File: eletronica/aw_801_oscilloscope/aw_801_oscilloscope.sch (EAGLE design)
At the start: 2 parts

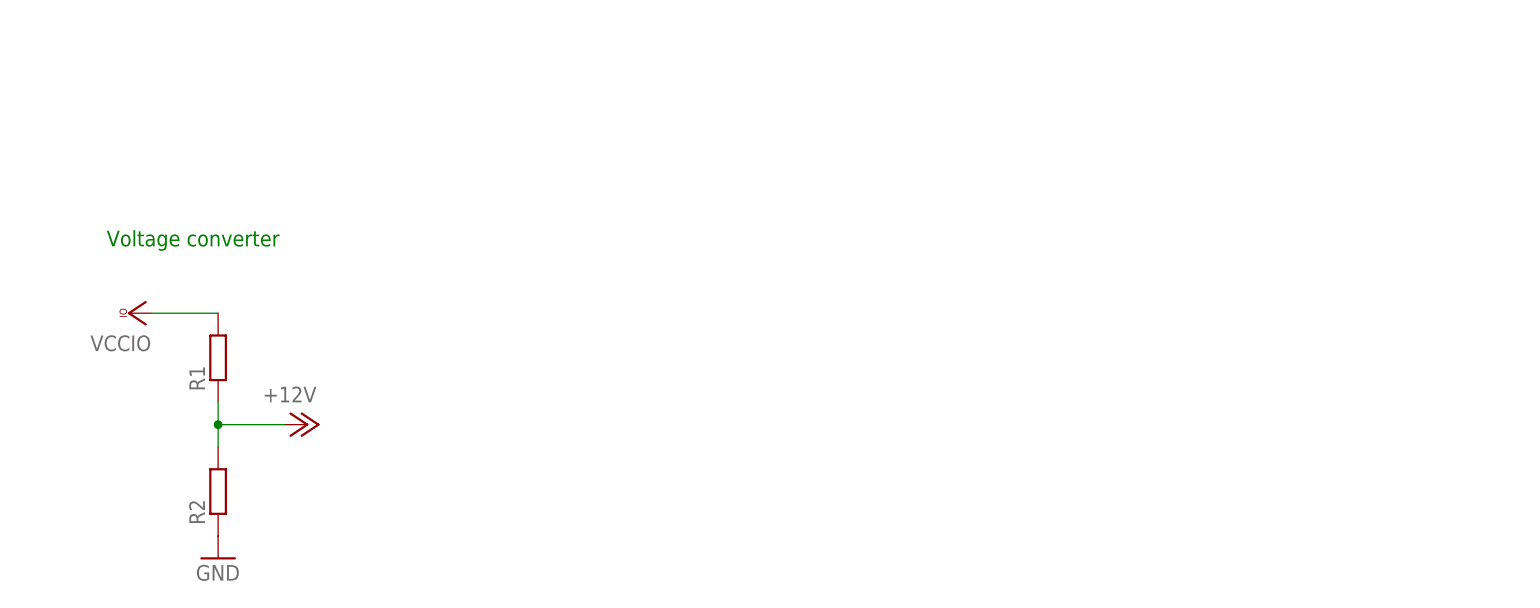
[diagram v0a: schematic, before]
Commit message: 
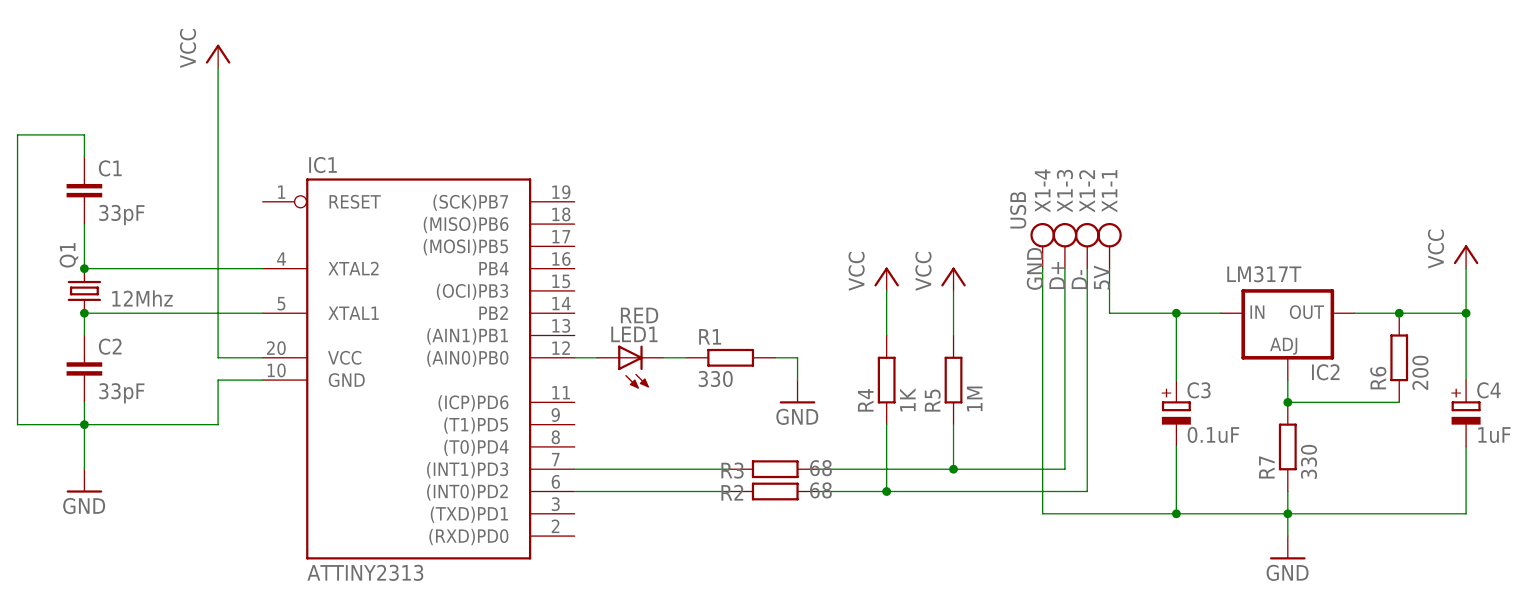
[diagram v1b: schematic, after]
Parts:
- added C1, C2: 33pF, rcl:C-EU050-030X075
- added C3: 0.1uF, rcl:CPOL-EUE2.5-6
- added C4: 1uF, rcl:CPOL-EUE2.5-6
- added IC1: ATTINY2313, atmel:AT90S2313P
- added IC2: LM317T, v-reg:LM317TS
- added LED1: RED, led:LED5MM
- added Q1: 12Mhz, crystal:CRYSTALHC49U70
- added R3: 68, rcl:R-EU_0207/10
- added R4: 1K, rcl:R-EU_0207/10
- added R5: 1M, rcl:R-EU_0207/10
- added R6: 200, rcl:R-EU_0207/10
- added R7: 330, rcl:R-EU_0207/10
- added X1: USB, con-ptr500:AK500/4
- R1: value (none) -> 330; device rcl:R-EU_0207/7 -> rcl:R-EU_0207/10
- R2: value (none) -> 68; device rcl:R-EU_0207/7 -> rcl:R-EU_0207/10
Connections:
- removed net +12V: R1.1, R2.2
- removed net VCCIO: R1.2
- new net 5V: C3.+, IC2.IN, X1-1.KL
- new net D+: R3.2, R5.1, X1-3.KL
- new net D-: R2.2, R4.1, X1-2.KL
- new net N$1: C1.2, IC1.XTAL2, Q1.2
- new net N$2: C2.1, IC1.XTAL1, Q1.1
- new net N$3: IC1.(AIN0)PB0, LED1.A
- new net N$4: LED1.C, R1.1
- new net N$5: IC1.(INT0)PD2, R2.1
- new net N$6: IC1.(INT1)PD3, R3.1
- new net N$9: IC2.ADJ, R6.1, R7.2
- new net VCC: C4.+, IC1.VCC, IC2.OUT, R4.2, R5.2, R6.2
- net GND: now also C1.1, C2.2, C3.-, C4.-, IC1.GND, R1.2, R7.1, X1-4.KL; no longer R2.1
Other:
- note removed: "Voltage converter"
- moved on the sheet: R1, R2

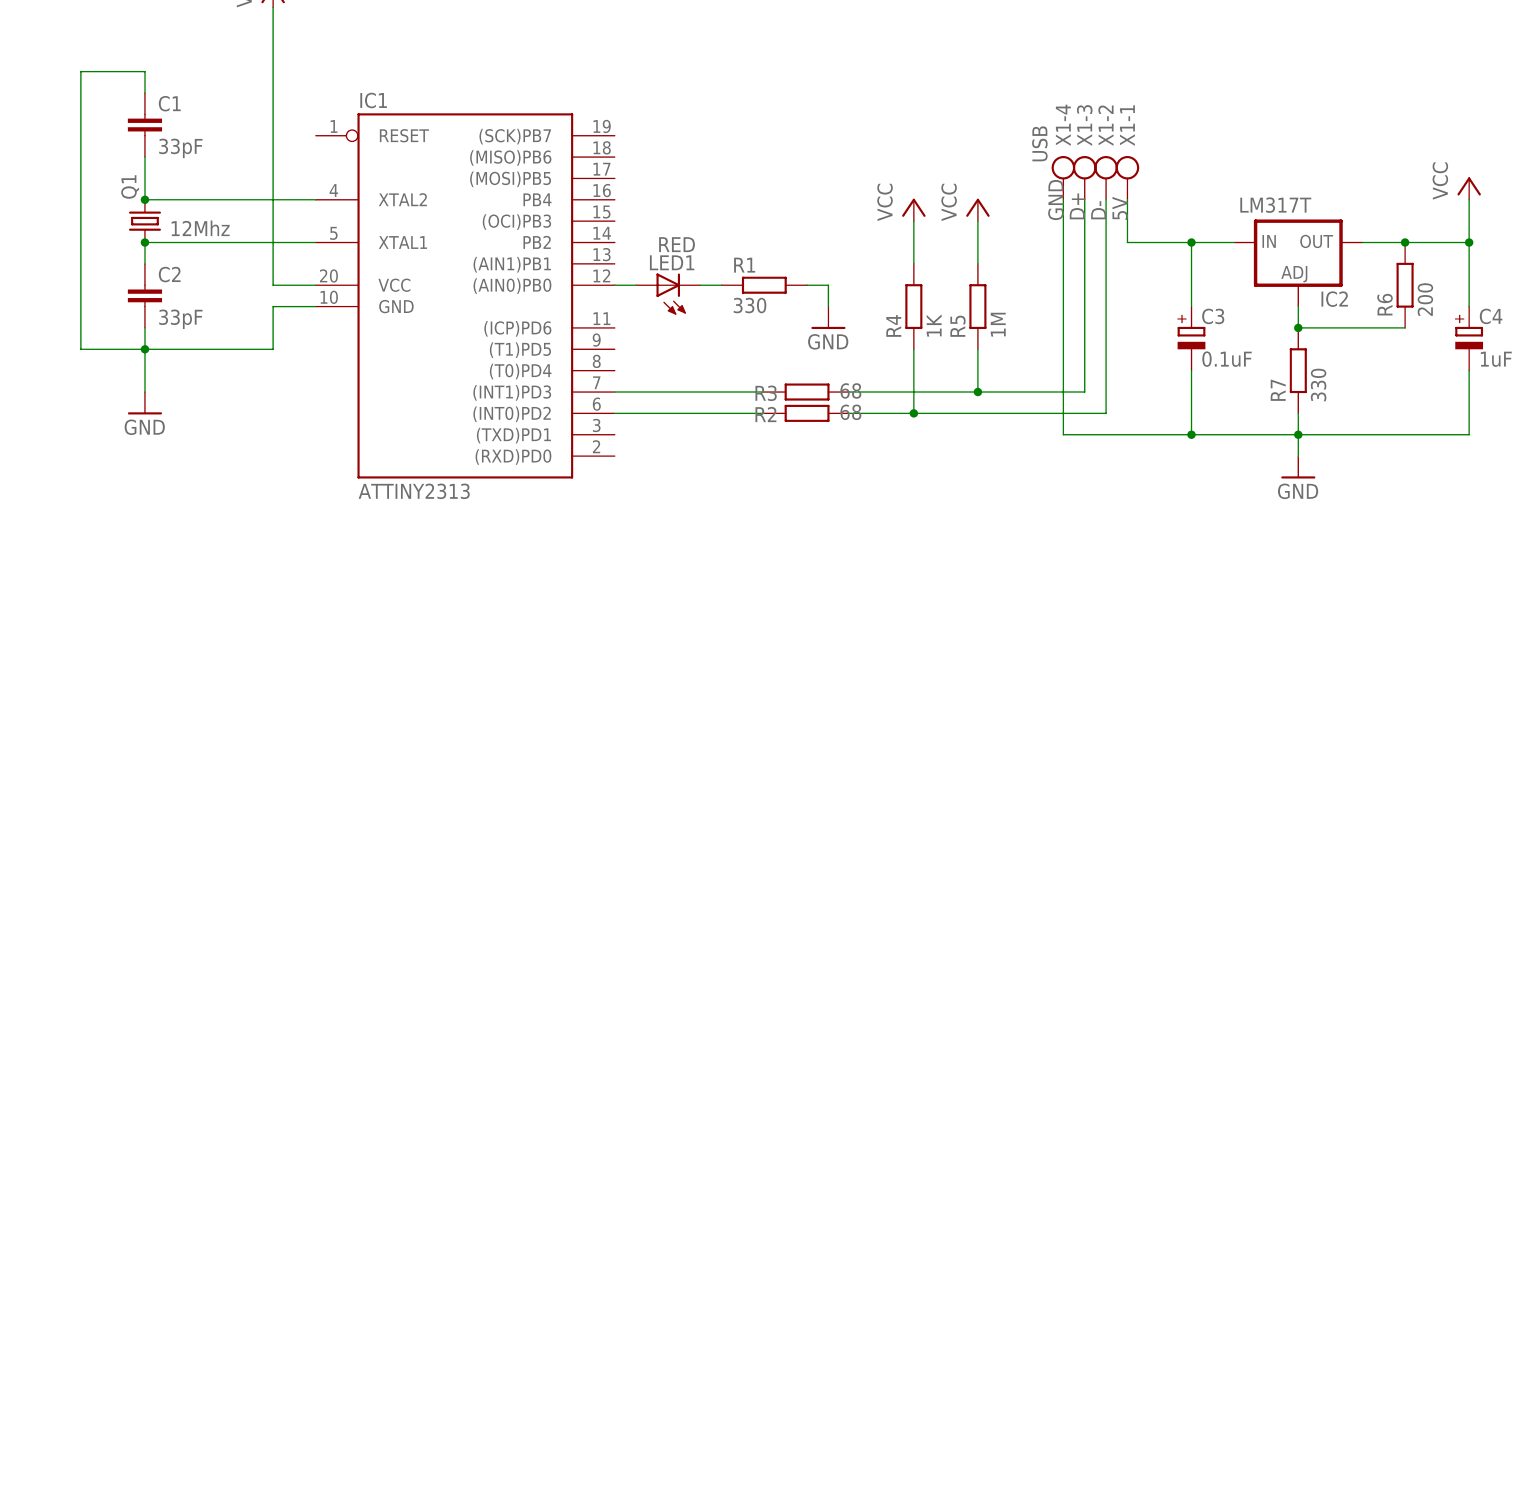
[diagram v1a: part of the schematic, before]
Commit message: 
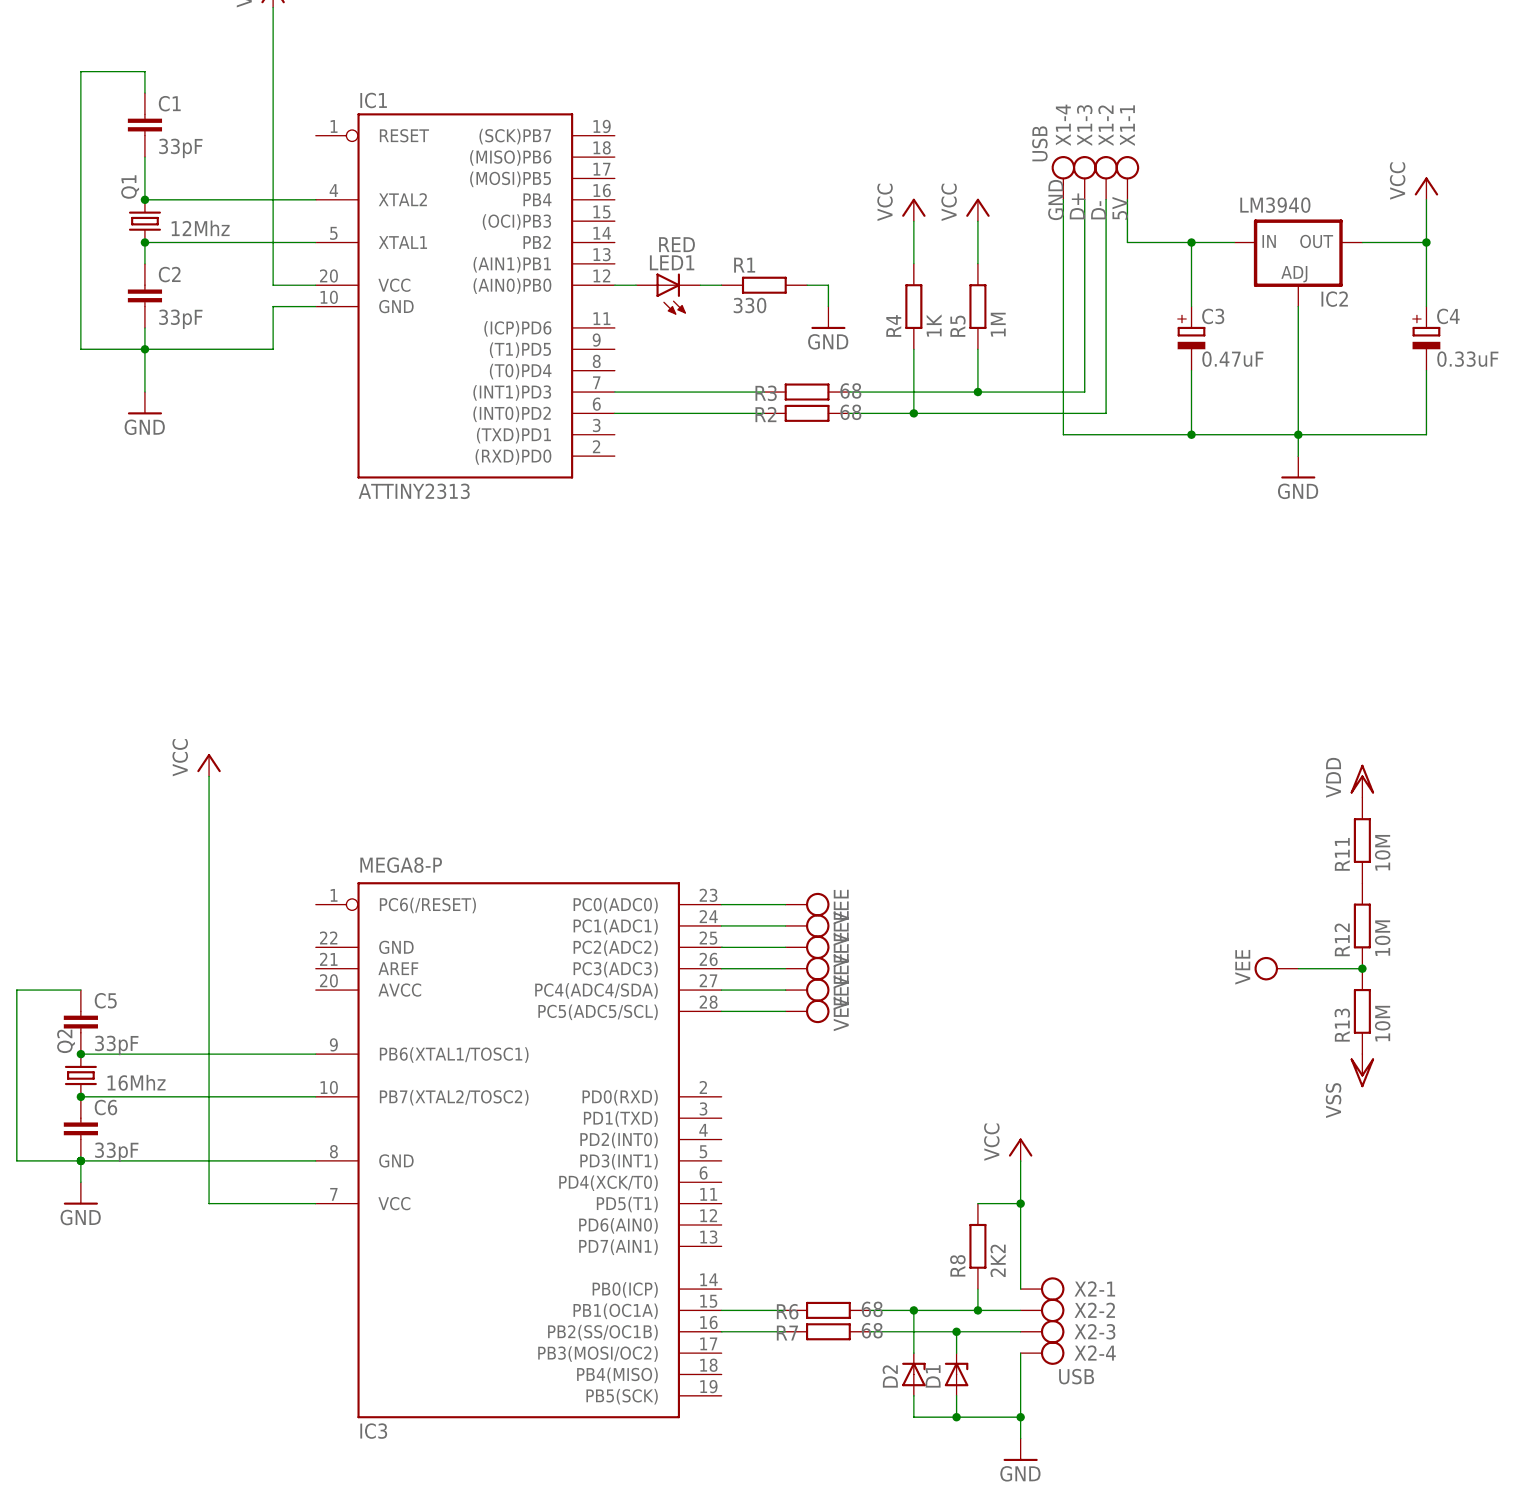
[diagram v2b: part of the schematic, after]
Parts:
- added C5, C6: 33pF, rcl:C-EU050-030X075
- added D1, D2: (no value), diode:ZENER-DIODEDO35Z10
- added IC3: MEGA8-P, atmel:MEGA8-P
- added Q2: 16Mhz, crystal:CRYSTALHC49U70
- added R11, R12, R13: 10M, rcl:R-EU_0207/10
- added R8: 2K2, rcl:R-EU_0207/10
- added X2: USB, con-ptr500:AK500/4
- C3: value 0.1uF -> 0.47uF
- C4: value 1uF -> 0.33uF
- IC2: value LM317T -> LM3940
- R6: value 200 -> 68
- R7: value 330 -> 68
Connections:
- new net N$10: D1.C, R7.2, X2-3.KL
- new net N$11: IC3.PB1(OC1A), R6.1
- new net N$12: IC3.PB2(SS/OC1B), R7.1
- new net N$15: R11.1, R12.2
- new net N$7: C5.2, IC3.PB6(XTAL1/TOSC1), Q2.2
- new net N$8: C6.1, IC3.PB7(XTAL2/TOSC2), Q2.1
- new net VDD: R11.2
- new net VEE: IC3.PC0(ADC0), IC3.PC1(ADC1), IC3.PC2(ADC2), IC3.PC3(ADC3), IC3.PC4(ADC4/SDA), IC3.PC5(ADC5/SCL), R12.1, R13.2
- new net VSS: R13.1
- net GND: now also C5.1, C6.2, D1.A, D2.A, IC2.ADJ, IC3.GND@1, X2-4.KL; no longer R7.1
- net N$9: now also D2.C, R6.2, R8.1, X2-2.KL; no longer IC2.ADJ, R6.1, R7.2
- net VCC: now also IC3.VCC@1, R8.2, X2-1.KL; no longer R6.2
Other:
- moved on the sheet: C4, R6, R7
